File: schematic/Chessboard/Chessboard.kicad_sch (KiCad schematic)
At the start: 7 parts, among them Q1 BC640, U1 5V-3.3V

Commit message: edit schematics
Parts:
- removed A1: Arduino_Nano_ESP32, Module:Arduino_Nano, symbol MCU_Module:Arduino_Nano_Every
- removed D1: WS2812B, LED_SMD:LED_WS2812B_PLCC4_5.0x5.0mm_P3.2mm, symbol LED:WS2812B
- removed H1: SS49E, Package_TO_SOT_THT:TO-92_Inline, symbol Sensor_Magnetic:DRV5033AJxLPG
- removed U1: 5V-3.3V, Converter_DCDC:Converter_DCDC_Murata_OKI-78SR_Vertical, symbol Converter_DCDC:OKI-78SR-3.3_1.5-W36-C
- added A2: Arduino_Nano_ESP32, Module:Arduino_Nano, symbol MCU_Module:Arduino_Nano_ESP32
- added C3: C_Polarized, Capacitor_THT:CP_Radial_D14.0mm_P5.00mm, symbol Device:C_Polarized
- added J1: LED, Connector_JST:JST_XH_B3B-XH-A_1x03_P2.50mm_Vertical, symbol Connector:Conn_01x03_Socket
- added J2, J4: VOUT, Connector_JST:JST_XH_B4B-XH-A_1x04_P2.50mm_Vertical, symbol Connector:Conn_01x04_Socket
- added J3: Data, Connector_JST:JST_XH_B5B-XH-A_1x05_P2.50mm_Vertical, symbol Connector:Conn_01x05_Socket
- added J5: Data, Connector_JST:JST_XH_B4B-XH-A_1x04_P2.50mm_Vertical, symbol Connector:Conn_01x04_Socket
- added Q2, Q3, Q4, Q5, Q6, Q7, Q8: BC640, Package_TO_SOT_THT:TO-92_Inline, symbol Transistor_BJT:BC636
- added R3, R4, R5, R6, R7, R8: 2K2, Resistor_THT:R_Axial_DIN0207_L6.3mm_D2.5mm_P10.16mm_Horizontal, symbol Device:R
- added SW1: SW_SPST, Connector_PinHeader_2.54mm:PinHeader_1x02_P2.54mm_Vertical, symbol Switch:SW_SPST
- added U1, U3, U4, U5: Logic Level Shifter, Library:LogicLevel4ch, symbol Library:BSS138_4ch
- added U2: Batterie Shield, Library:D1_mini_board, symbol Library:WeMos_mini
- R1: value 10K -> 2K2
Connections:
- net +3V3: now also A2.17 (3V3), U1.10 (LV), U3.10 (LV), U4.10 (LV), U5.10 (LV); no longer Q1.1 (E)
- net +5V: now also Q1.1 (E), A2.30 (VIN), C3.1, J1.1 (Pin_1), Q2.1 (E), Q3.1 (E), Q4.1 (E), Q5.1 (E), Q6.1 (E), Q7.1 (E), Q8.1 (E), SW1.1 (A), U1.3 (HV), U3.3 (HV), U4.3 (HV), U5.3 (HV)
- net GND: now also A2.29 (GND), A2.4 (GND), C3.2, J1.3 (Pin_3), J3.1 (Pin_1), U1.4 (GND), U1.9 (GND), U2.2 (GND), U3.4 (GND), U3.9 (GND), U4.4 (GND), U4.9 (GND), U5.4 (GND), U5.9 (GND); no longer R1.2
- net at R1.1: now also Q2.3 (B)
- net at R2.2: now also U3.1 (HV1)
- net Sensor/VS1: now reaches Q1.2 (C)
- net Sensor/VS1: now also J2.1 (Pin_1)
- new net: Q8.3 (B), R8.1
- new net: R8.2, U5.5 (HV3)
- new net: R6.2, U5.1 (HV1)
- new net: A2.11 (D8), U5.11 (LV2)
- new net: A2.10 (D7), U5.12 (LV1)
- new net: R5.2, U5.2 (HV2)
- new net: R7.2, U5.6 (HV4)
- new net: A2.13 (D10/CS), U5.7 (LV4)
- new net: A2.12 (D9), U5.8 (LV3)
- new net: A2.25 (A6), U1.11 (LV2)
- new net: A2.26 (A7), U1.12 (LV1)
- new net: A2.23 (SDA/A4), U1.7 (LV4)
- new net: A2.24 (SCL/A5), U1.8 (LV3)
- new net: Q3.3 (B), R3.1
- new net: A2.7 (D4), U3.11 (LV2)
- new net: A2.6 (D3), U3.12 (LV1)
- new net: R1.2, U3.2 (HV2)
- new net: R3.2, U3.5 (HV3)
- new net: R4.2, U3.6 (HV4)
- new net: A2.9 (D6), U3.7 (LV4)
- new net: A2.8 (D5), U3.8 (LV3)
- new net: Q4.3 (B), R4.1
- new net: A2.19 (A0), U4.7 (LV4)
- new net: A2.20 (A1), U4.8 (LV3)
- new net: A2.21 (A2), U4.11 (LV2)
- new net: A2.22 (A3), U4.12 (LV1)
- new net: Q5.3 (B), R5.1
- new net: Q6.3 (B), R6.1
- new net: SW1.2 (B), U2.1 (5V)
- new net: Q7.3 (B), R7.1
- new net LED/LED_Data: A2.5 (D2), J1.2 (Pin_2)
- new net Sensor/D1: J3.2 (Pin_2), U1.1 (HV1)
- new net Sensor/D2: J3.3 (Pin_3), U1.2 (HV2)
- new net Sensor/D3: J3.4 (Pin_4), U1.5 (HV3)
- new net Sensor/D4: J3.5 (Pin_5), U1.6 (HV4)
- new net Sensor/D5: J5.1 (Pin_1), U4.1 (HV1)
- new net Sensor/D6: J5.2 (Pin_2), U4.2 (HV2)
- new net Sensor/D7: J5.3 (Pin_3), U4.5 (HV3)
- new net Sensor/D8: J5.4 (Pin_4), U4.6 (HV4)
- new net Sensor/VS2: J2.2 (Pin_2), Q2.2 (C)
- new net Sensor/VS3: J2.3 (Pin_3), Q3.2 (C)
- new net Sensor/VS4: J2.4 (Pin_4), Q4.2 (C)
- new net Sensor/VS5: J4.1 (Pin_1), Q6.2 (C)
- new net Sensor/VS6: J4.2 (Pin_2), Q5.2 (C)
- new net Sensor/VS7: J4.3 (Pin_3), Q8.2 (C)
- new net Sensor/VS8: J4.4 (Pin_4), Q7.2 (C)
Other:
- added sheet LED (LED.kicad_sch)
- added sheet Sensor (Sensor.kicad_sch)
- moved on the sheet: Q1, R2

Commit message: routen and gerber files
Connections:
- net Sensor/VS5: now also Q5.2 (C); no longer Q6.2 (C)
- net Sensor/VS6: now also Q6.2 (C); no longer Q5.2 (C)
- net Sensor/VS7: now also Q7.2 (C); no longer Q8.2 (C)
- net Sensor/VS8: now also Q8.2 (C); no longer Q7.2 (C)
- net at Q2.3 (B): now also R2.1; no longer R1.1
- net at R8.2: now also U5.6 (HV4); no longer U5.5 (HV3)
- net at U5.1 (HV1): now also R5.2; no longer R6.2
- net at U5.2 (HV2): now also R6.2; no longer R5.2
- net at R7.2: now also U5.5 (HV3); no longer U5.6 (HV4)
- net at U1.11 (LV2): now also A2.20 (A1); no longer A2.25 (A6)
- net at U1.12 (LV1): now also A2.19 (A0); no longer A2.26 (A7)
- net at U1.7 (LV4): now also A2.22 (A3); no longer A2.23 (SDA/A4)
- net at U1.8 (LV3): now also A2.21 (A2); no longer A2.24 (SCL/A5)
- net at Q1.3 (B): now also R1.1; no longer R2.1
- net at R2.2: now also U3.2 (HV2); no longer U3.1 (HV1)
- net at R1.2: now also U3.1 (HV1); no longer U3.2 (HV2)
- net at U4.7 (LV4): now also A2.26 (A7); no longer A2.19 (A0)
- net at U4.8 (LV3): now also A2.25 (A6); no longer A2.20 (A1)
- net at U4.11 (LV2): now also A2.24 (SCL/A5); no longer A2.21 (A2)
- net at U4.12 (LV1): now also A2.23 (SDA/A4); no longer A2.22 (A3)
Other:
- sheet LED renamed LED_ROW_1_2
- sheet LED_ROW_1_2: file LED.kicad_sch -> LED_ROW_1_2.kicad_sch
- moved on the sheet: C3, J1, J3, J5, Q5, Q6, Q7, Q8, R1, R2, R3, R4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

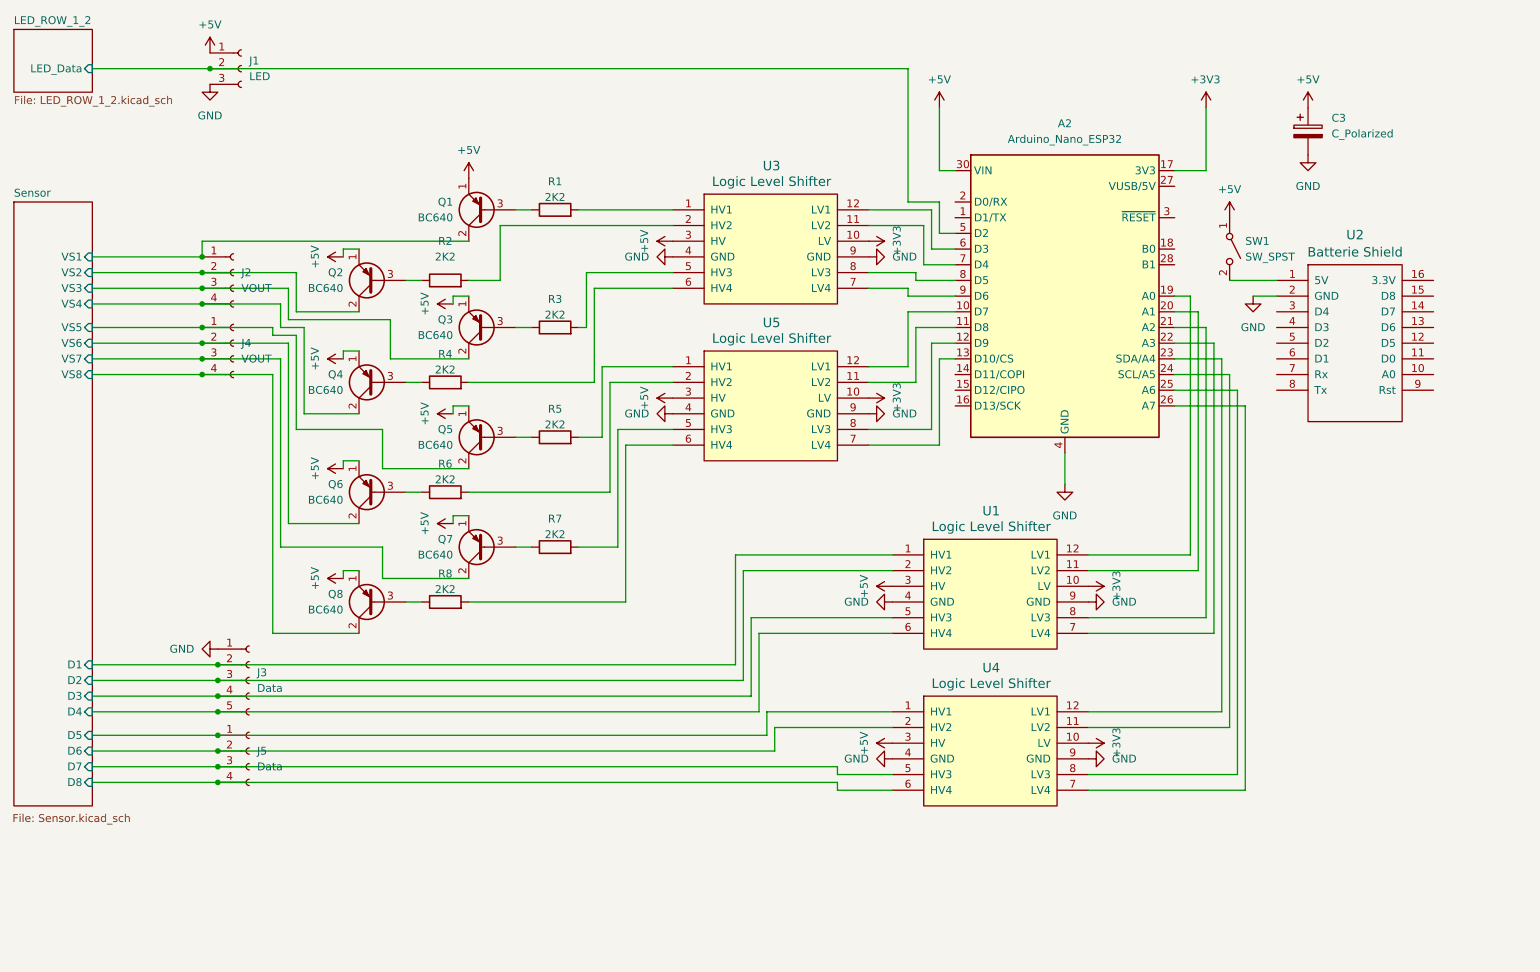
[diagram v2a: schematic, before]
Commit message: add left and right input field
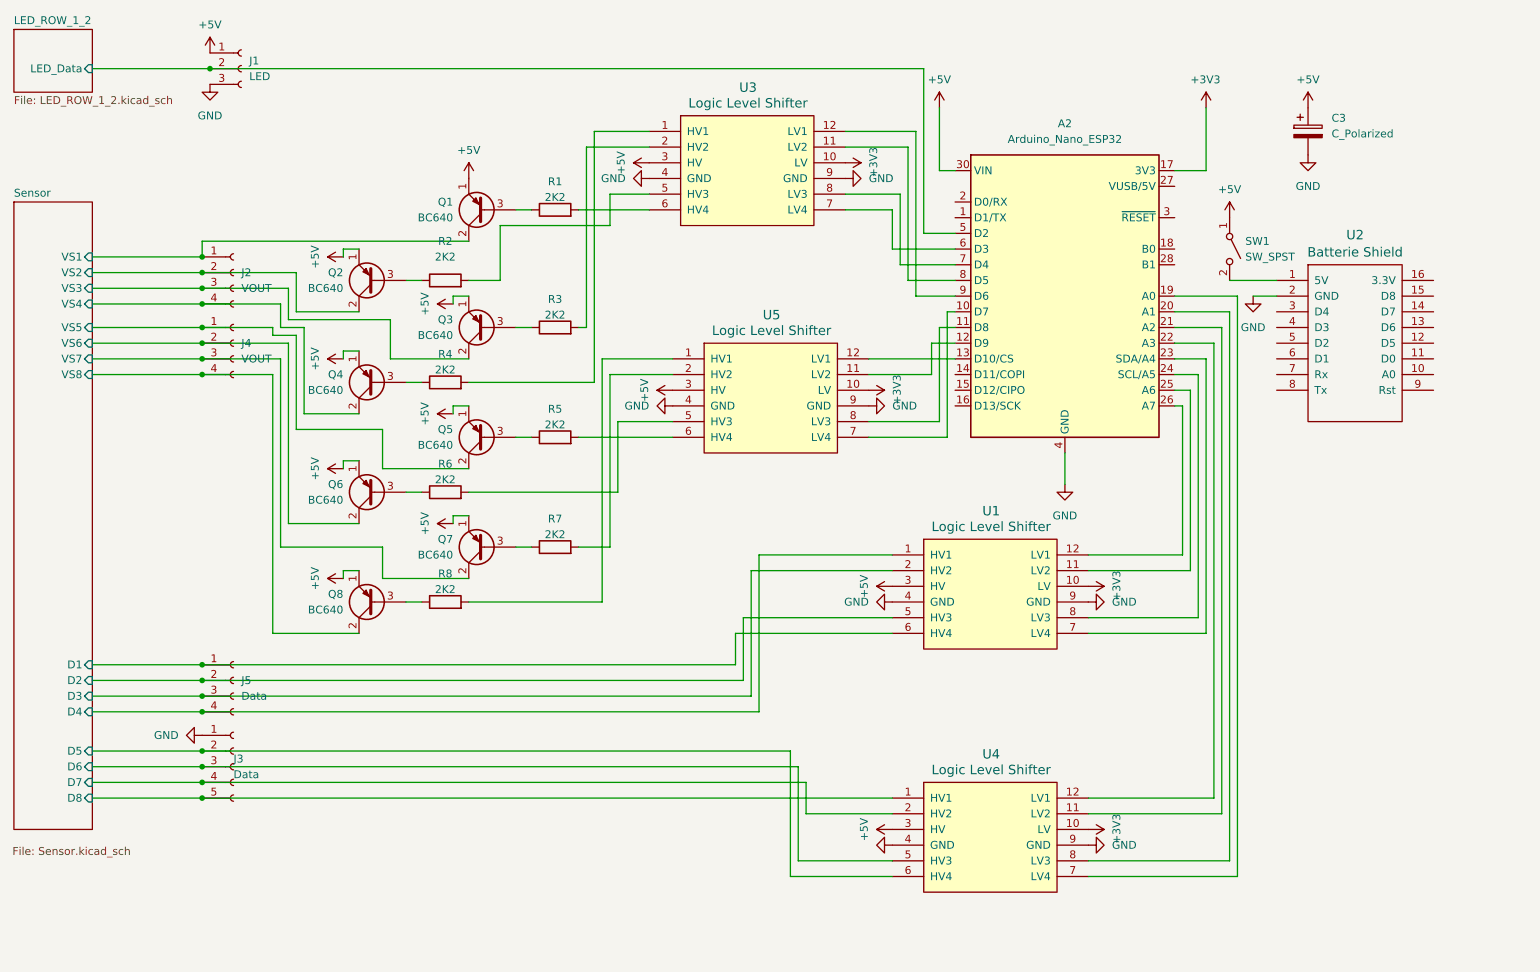
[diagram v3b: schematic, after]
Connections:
- net Sensor/D1: now also J5.1 (Pin_1), U1.6 (HV4); no longer J3.2 (Pin_2), U1.1 (HV1)
- net Sensor/D2: now also J5.2 (Pin_2), U1.5 (HV3); no longer J3.3 (Pin_3), U1.2 (HV2)
- net Sensor/D3: now also J5.3 (Pin_3), U1.2 (HV2); no longer J3.4 (Pin_4), U1.5 (HV3)
- net Sensor/D4: now also J5.4 (Pin_4), U1.1 (HV1); no longer J3.5 (Pin_5), U1.6 (HV4)
- net Sensor/D5: now also J3.2 (Pin_2), U4.6 (HV4); no longer J5.1 (Pin_1), U4.1 (HV1)
- net Sensor/D6: now also J3.3 (Pin_3), U4.5 (HV3); no longer J5.2 (Pin_2), U4.2 (HV2)
- net Sensor/D7: now also J3.4 (Pin_4), U4.2 (HV2); no longer J5.3 (Pin_3), U4.5 (HV3)
- net Sensor/D8: now also J3.5 (Pin_5), U4.1 (HV1); no longer J5.4 (Pin_4), U4.6 (HV4)
- net at R8.2: now also U5.1 (HV1); no longer U5.6 (HV4)
- net at R5.2: now also U5.6 (HV4); no longer U5.1 (HV1)
- net at U5.11 (LV2): now also A2.12 (D9); no longer A2.11 (D8)
- net at U5.12 (LV1): now also A2.13 (D10/CS); no longer A2.10 (D7)
- net at U5.2 (HV2): now also R7.2; no longer R6.2
- net at U5.5 (HV3): now also R6.2; no longer R7.2
- net at U5.7 (LV4): now also A2.10 (D7); no longer A2.13 (D10/CS)
- net at U5.8 (LV3): now also A2.11 (D8); no longer A2.12 (D9)
- net at U1.11 (LV2): now also A2.25 (A6); no longer A2.20 (A1)
- net at U1.12 (LV1): now also A2.26 (A7); no longer A2.19 (A0)
- net at U1.7 (LV4): now also A2.23 (SDA/A4); no longer A2.22 (A3)
- net at U1.8 (LV3): now also A2.24 (SCL/A5); no longer A2.21 (A2)
- net at R2.2: now also U3.5 (HV3); no longer U3.2 (HV2)
- net at U3.1 (HV1): now also R4.2; no longer R1.2
- net at U3.11 (LV2): now also A2.8 (D5); no longer A2.7 (D4)
- net at U3.12 (LV1): now also A2.9 (D6); no longer A2.6 (D3)
- net at R3.2: now also U3.2 (HV2); no longer U3.5 (HV3)
- net at U3.6 (HV4): now also R1.2; no longer R4.2
- net at U3.7 (LV4): now also A2.6 (D3); no longer A2.9 (D6)
- net at U3.8 (LV3): now also A2.7 (D4); no longer A2.8 (D5)
- net at U4.12 (LV1): now also A2.22 (A3); no longer A2.23 (SDA/A4)
- net at U4.11 (LV2): now also A2.21 (A2); no longer A2.24 (SCL/A5)
- net at U4.8 (LV3): now also A2.20 (A1); no longer A2.25 (A6)
- net at U4.7 (LV4): now also A2.19 (A0); no longer A2.26 (A7)
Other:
- moved on the sheet: J3, J5, U3, U4, U5
